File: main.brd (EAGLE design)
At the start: 42.9 x 27.9 mm, 49 parts, among them IC1 MEGA8-AI, IC2 MCP73831, IC3 7805DT, Q2 32768k

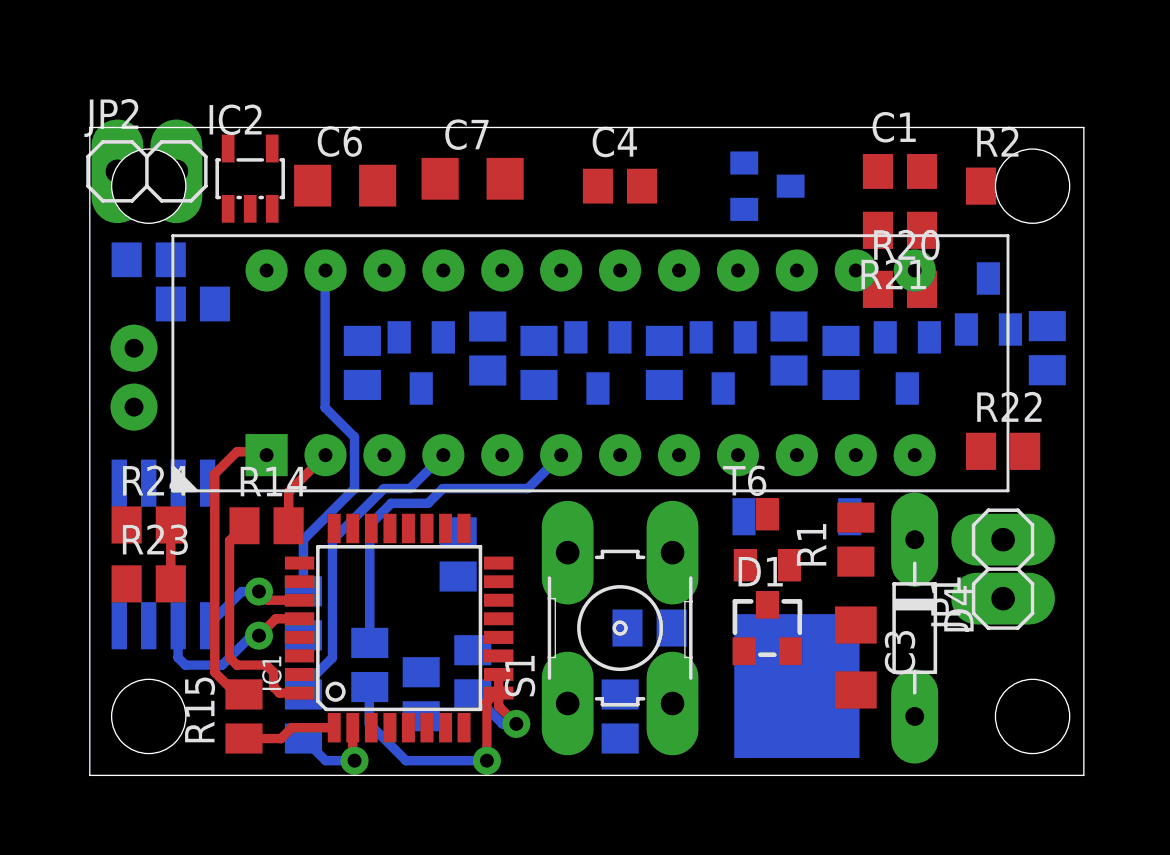
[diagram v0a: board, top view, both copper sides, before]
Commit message: Shift digit common pins Fix digit common pins
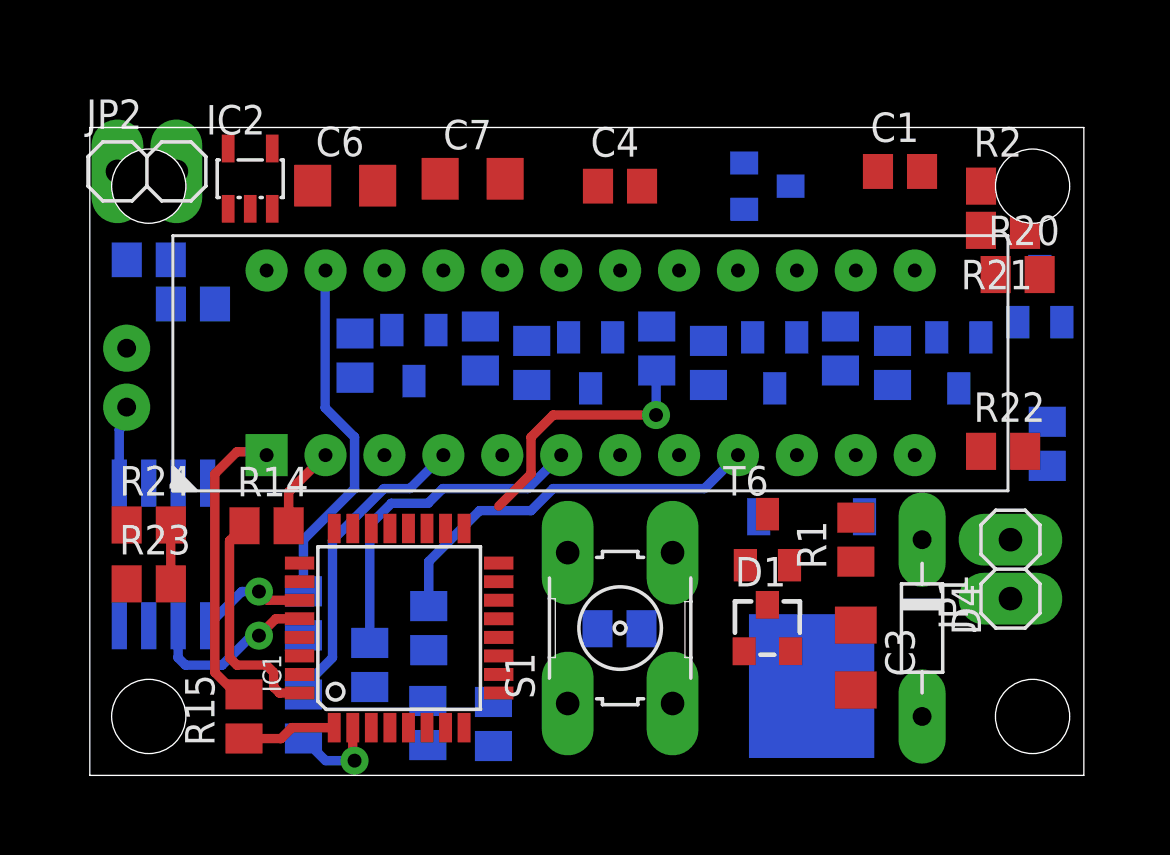
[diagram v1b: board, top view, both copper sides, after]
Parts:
- moved R6 12.3 mm to (24.4, 18.4)
- moved R4 10.4 mm to (14.6, 2.26), turned to 90 degrees
- moved R19 9.00 mm to (22.8, 6.32), turned to 180 degrees
- moved R3 5.47 mm to (17.4, 2.21), turned to 270 degrees
- moved R20 5.11 mm to (40.0, 21.6)
- moved R21 4.44 mm to (39.4, 23.5)
- moved R8 4.12 mm to (41.3, 14.3)
- moved R18 2.69 mm to (14.6, 6.35)
- moved T1 2.24 mm to (41.0, 20.6)
- moved R12 2.22 mm to (34.6, 17.8)
- moved T4 2.22 mm to (29.5, 17.8)
- moved T5 2.22 mm to (37.5, 17.8)
- moved R7 2.22 mm to (32.4, 18.4)
- moved R11 1.90 mm to (26.7, 17.8)
- moved IC3 0.63 mm to (31.1, 6.35)
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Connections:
- net N$23: now also IC1.12; no longer IC1.13
- net N$24: now also IC1.13; no longer IC1.14
- net N$25: now also IC1.16; no longer IC1.17
- net N$26: now also IC1.15; no longer IC1.16
- net N$27: now also IC1.14; no longer IC1.15
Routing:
- net N$32: track 0.00 -> 17.2 mm
- net N$26: track 0.00 -> 11.3 mm, vias 0 -> 1
- net N$19: track 10.5 -> 0.00 mm, vias 1 -> 0
- net N$35: track 4.85 -> 0.00 mm, vias 1 -> 0
- net N$29: track 0.00 -> 3.41 mm

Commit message: Schematics and PCB
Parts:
- moved R2 33.0 mm to (7.25, 17.8), turned to 90 degrees
- moved R21 23.2 mm to (28.2, 3.12), turned to 90 degrees
- moved D2 19.5 mm to (32.0, 6.06), flipped to the top
- moved R22 18.3 mm to (23.5, 4.82), flipped to the bottom, turned to 90 degrees
- moved R20 17.9 mm to (29.1, 7.35), turned to 90 degrees
- moved C1 16.5 mm to (29.2, 10.5)
- moved R4 14.7 mm to (16.5, 16.8), flipped to the top
- moved R19 12.2 mm to (30.4, 15.9), flipped to the top, turned to 0 degrees
- moved D4 12.1 mm to (41.3, 17.1)
- moved IC2 9.42 mm to (12.3, 18.0), turned to 90 degrees
- moved C6 8.69 mm to (3.26, 21.5), turned to 180 degrees
- moved T6 7.33 mm to (35.5, 6.32), turned to 180 degrees
- moved T1 6.34 mm to (35.9, 16.8)
- moved R3 6.04 mm to (17.2, 8.25), turned to 90 degrees
- moved JP2 5.75 mm to (8.20, 25.6), turned to 90 degrees
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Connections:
- net N$19: now also IC1.10; no longer IC1.9
- net N$24: now also IC1.17
- net N$28: now also Q2.1; no longer Q2.2
- net N$29: now also Q2.2; no longer Q2.1
- net N$3: now also IC1.19; no longer IC1.22
- net N$30: now also IC1.31
- net N$35: now also IC1.9; no longer IC1.10
- net N$38: now also IC1.23; no longer IC1.19
- net N$4: now also IC1.24; no longer IC1.23
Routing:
- net +5V: track 2.54 -> 114.7 mm, vias 0 -> 1
- net GND: track 0.00 -> 72.5 mm
- net N$38: track 0.00 -> 40.5 mm, vias 0 -> 2
- net N$33: track 0.00 -> 36.8 mm
- net N$13: track 0.00 -> 33.8 mm
- net N$3: track 0.00 -> 31.6 mm
- net +12V: track 0.00 -> 30.7 mm
- net N$34: track 15.3 -> 40.4 mm
- net N$7: track 0.00 -> 21.7 mm, vias 0 -> 2
- net N$1: track 3.70 -> 24.2 mm
- net N$36: track 0.00 -> 19.8 mm
- net N$32: track 17.2 -> 36.5 mm
- net N$27: track 0.00 -> 19.1 mm
- net VDD: track 0.00 -> 18.8 mm
- net N$12: track 0.00 -> 17.8 mm
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
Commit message: PCB
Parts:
- moved C4 4.75 mm to (19.4, 28.3)
- moved R19 2.54 mm to (33.0, 15.9)
- moved R7 2.29 mm to (26.6, 16.2)
- moved JP2 0.95 mm to (7.25, 25.6)
- moved C7 0.90 mm to (13.3, 26.4)
- moved R2 0.32 mm to (7.25, 17.5)
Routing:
- net N$12: track 17.8 -> 36.4 mm
- net +5V: track 114.7 -> 129.5 mm
- net GND: track 72.5 -> 63.5 mm
- net VDD: track 18.8 -> 25.6 mm
- net N$27: track 19.1 -> 16.3 mm
- net N$33: track 36.8 -> 34.3 mm
- net N$36: track 19.8 -> 22.2 mm
- net N$17: track 8.47 -> 10.1 mm
- net N$34: track 40.4 -> 38.9 mm
- net N$1: track 24.2 -> 22.8 mm
- net N$32: track 36.5 -> 35.7 mm
- net N$6: track 9.64 -> 9.13 mm
